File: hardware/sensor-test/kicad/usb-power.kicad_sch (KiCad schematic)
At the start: 12 parts, among them J1 TYPE-C-31-M-12, U10 USBLC6-2SC6, U3 AP2112K-3.3TRG1

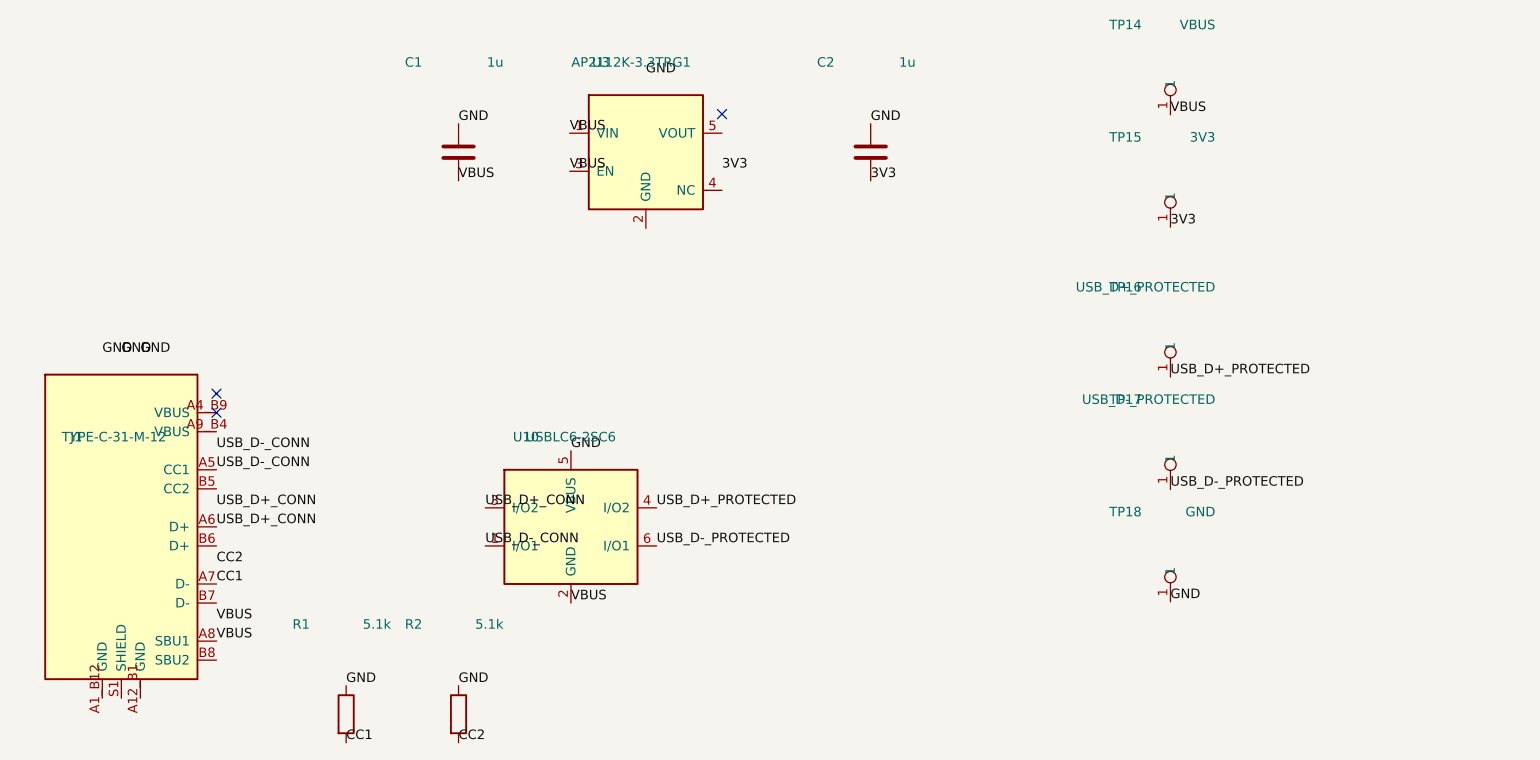
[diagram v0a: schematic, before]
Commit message: Fix USB-C pin coordinates and ERC power source
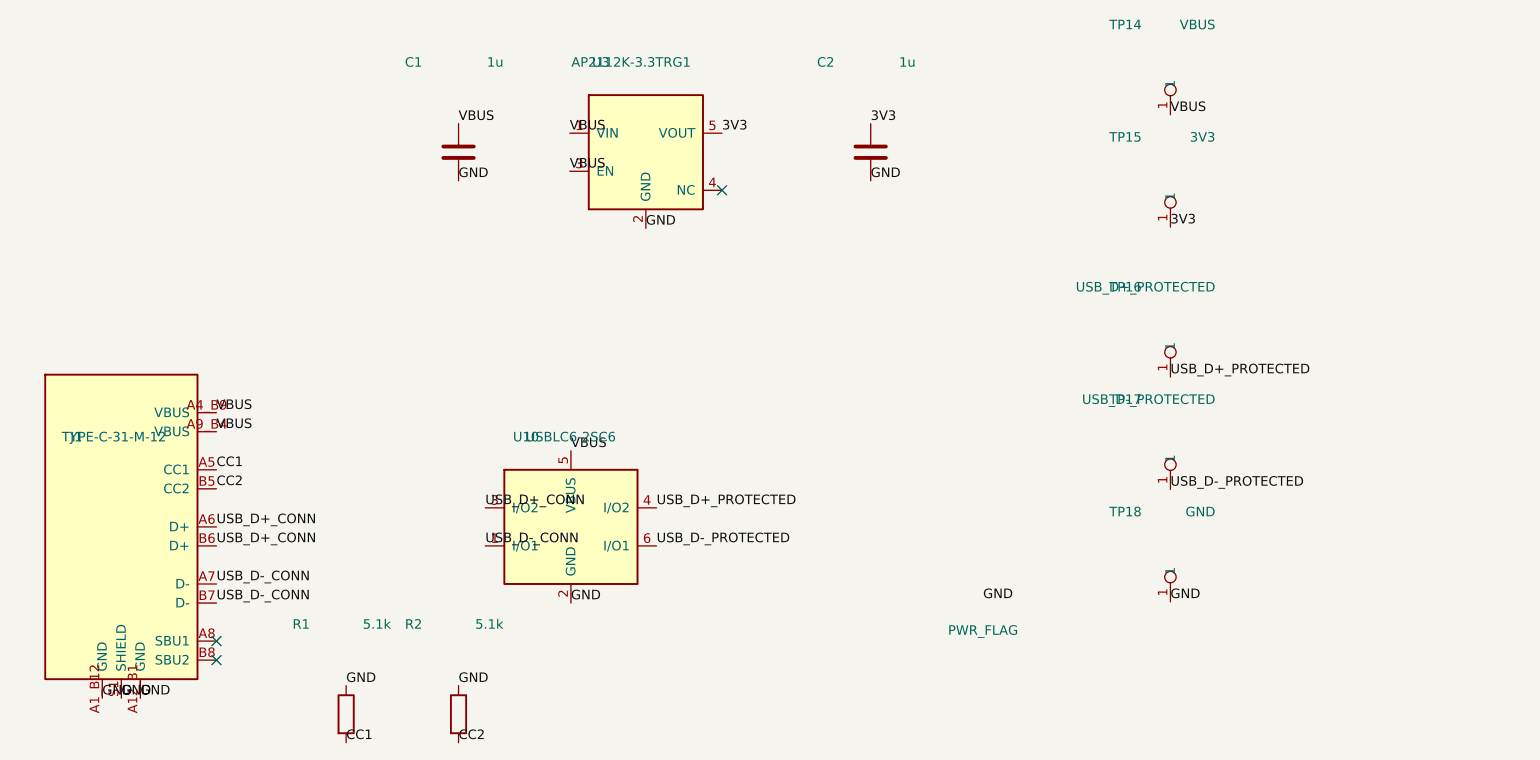
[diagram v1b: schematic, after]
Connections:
- net 3V3: now also C2.1, U3.5 (VOUT); no longer C2.2
- net CC1: now also J1.A5 (CC1); no longer J1.A7 (D-)
- net CC2: now also J1.B5 (CC2)
- net GND: now also C1.2, C2.2, J1.A12_B1 (GND), J1.A1_B12 (GND), J1.S1 (SHIELD), U10.2 (GND), U3.2 (GND); no longer C1.1, C2.1, U10.5 (VBUS)
- net USB_D+_CONN: now also J1.B6 (D+)
- net USB_D-_CONN: now also J1.A7 (D-), J1.B7 (D-); no longer J1.A5 (CC1)
- net VBUS: now also C1.1, J1.A4_B9 (VBUS), J1.A9_B4 (VBUS), U10.5 (VBUS); no longer C1.2, J1.A8 (SBU1), U10.2 (GND)
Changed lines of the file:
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@@
     (company "HE Piantor 42")
   )
-  (no_connect (at 57.7 84.76))
-  (no_connect (at 57.7 82.22))
-  (no_connect (at 125.16 44.92))
-  (label "VBUS" (at 57.7 115.24 0) (effects (font (size 1.27 1.27)) (justify left bottom)))
-  (label "VBUS" (at 57.7 112.7 0) (effects (font (size 1.27 1.27)) (justify left bottom)))
-  (label "CC1" (at 57.7 107.62 0) (effects (font (size 1.27 1.27)) (justify left bottom)))
-  (label "CC2" (at 57.7 105.08 0) (effects (font (size 1.27 1.27)) (justify left bottom)))
+  (no_connect (at 57.7 115.24))
+  (no_connect (at 57.7 117.78))
+  (no_connect (at 125.16 55.08))
+  (label "VBUS" (at 57.7 84.76 0) (effects (font (size 1.27 1.27)) (justify left bottom)))
+  (label "VBUS" (at 57.7 87.3 0) (effects (font (size 1.27 1.27)) (justify left bottom)))
+  (label "CC1" (at 57.7 92.38 0) (effects (font (size 1.27 1.27)) (justify left bottom)))
+  (label "CC2" (at 57.7 94.92 0) (effects (font (size 1.27 1.27)) (justify left bottom)))
   (label "USB_D+_CONN" (at 57.7 100 0) (effects (font (size 1.27 1.27)) (justify left bottom)))
-  (label "USB_D+_CONN" (at 57.7 97.46 0) (effects (font (size 1.27 1.27)) (justify left bottom)))
-  (label "USB_D-_CONN" (at 57.7 92.38 0) (effects (font (size 1.27 1.27)) (justify left bottom)))
-  (label "USB_D-_CONN" (at 57.7 89.84 0) (effects (font (size 1.27 1.27)) (justify left bottom)))
-  (label "GND" (at 42.46 77.14 0) (effects (font (size 1.27 1.27)) (justify left bottom)))
-  (label "GND" (at 47.54 77.14 0) (effects (font (size 1.27 1.27)) (justify left bottom)))
-  (label "GND" (at 45 77.14 0) (effects (font (size 1.27 1.27)) (justify left bottom)))
+  (label "USB_D+_CONN" (at 57.7 102.54 0) (effects (font (size 1.27 1.27)) (justify left bottom)))
+  (label "USB_D-_CONN" (at 57.7 107.62 0) (effects (font (size 1.27 1.27)) (justify left bottom)))
+  (label "USB_D-_CONN" (at 57.7 110.16 0) (effects (font (size 1.27 1.27)) (justify left bottom)))
+  (label "GND" (at 42.46 122.86 0) (effects (font (size 1.27 1.27)) (justify left bottom)))
+  (label "GND" (at 47.54 122.86 0) (effects (font (size 1.27 1.27)) (justify left bottom)))
+  (label "GND" (at 45 122.86 0) (effects (font (size 1.27 1.27)) (justify left bottom)))
   (label "CC1" (at 75 128.81 0) (effects (font (size 1.27 1.27)) (justify left bottom)))
   (label "GND" (at 75 121.19 0) (effects (font (size 1.27 1.27)) (justify left bottom)))
@@
   (label "USB_D-_CONN" (at 93.57 102.54 0) (effects (font (size 1.27 1.27)) (justify left bottom)))
   (label "USB_D-_PROTECTED" (at 116.43 102.54 0) (effects (font (size 1.27 1.27)) (justify left bottom)))
-  (label "VBUS" (at 105 110.16 0) (effects (font (size 1.27 1.27)) (justify left bottom)))
-  (label "GND" (at 105 89.84 0) (effects (font (size 1.27 1.27)) (justify left bottom)))
+  (label "VBUS" (at 105 89.84 0) (effects (font (size 1.27 1.27)) (justify left bottom)))
+  (label "GND" (at 105 110.16 0) (effects (font (size 1.27 1.27)) (justify left bottom)))
   (label "VBUS" (at 104.84 52.54 0) (effects (font (size 1.27 1.27)) (justify left bottom)))
   (label "VBUS" (at 104.84 47.46 0) (effects (font (size 1.27 1.27)) (justify left bottom)))
-  (label "GND" (at 115 39.84 0) (effects (font (size 1.27 1.27)) (justify left bottom)))
-  (label "3V3" (at 125.16 52.54 0) (effects (font (size 1.27 1.27)) (justify left bottom)))
-  (label "VBUS" (at 90 53.81 0) (effects (font (size 1.27 1.27)) (justify left bottom)))
-  (label "GND" (at 90 46.19 0) (effects (font (size 1.27 1.27)) (justify left bottom)))
-  (label "3V3" (at 145 53.81 0) (effects (font (size 1.27 1.27)) (justify left bottom)))
-  (label "GND" (at 145 46.19 0) (effects (font (size 1.27 1.27)) (justify left bottom)))
+  (label "GND" (at 115 60.16 0) (effects (font (size 1.27 1.27)) (justify left bottom)))
+  (label "3V3" (at 125.16 47.46 0) (effects (font (size 1.27 1.27)) (justify left bottom)))
+  (label "VBUS" (at 90 46.19 0) (effects (font (size 1.27 1.27)) (justify left bottom)))
+  (label "GND" (at 90 53.81 0) (effects (font (size 1.27 1.27)) (justify left bottom)))
+  (label "3V3" (at 145 46.19 0) (effects (font (size 1.27 1.27)) (justify left bottom)))
+  (label "GND" (at 145 53.81 0) (effects (font (size 1.27 1.27)) (justify left bottom)))
   (symbol (lib_id "HEP:HRO_TYPE-C-31-M-12") (at 45 100 0) (unit 1)
     (in_bom yes) (on_board yes) (dnp no)
@@
   )
   (label "GND" (at 185 110 0) (effects (font (size 1.27 1.27)) (justify left bottom)))
-  (sheet_instances
+(symbol (lib_id "power:PWR_FLAG") (at 160 110 0) (unit 1)
+    (in_bom yes) (on_board yes) (dnp no)
+    (property "Reference" "#FLG01" (at 160 111.905 0) (effects (font (size 1.27 1.27)) hide))
+    (property "Value" "PWR_FLAG" (at 160 113.81 0) (effects (font (size 1.27 1.27))))
+    (property "Footprint" "" (at 160 110 0) (effects (font (size 1.27 1.27)) hide))
+    (property "Datasheet" "~" (at 160 110 0) (effects (font (size 1.27 1.27)) hide))
+    (pin "1")
+    (instances
+      (project "usb-power"
+        (path "/c0000000-0000-0000-0000-000000000001"
+          (reference "#FLG01") (unit 1)
+        )
+      )
+    )
+  )
+  (label "GND" (at 160 110 0)
+    (effects (font (size 1.27 1.27)) (justify left bottom))
+  )
+    (sheet_instances
     (path "/" (page "1"))
   )

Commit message: Model USB VBUS source correctly for ERC
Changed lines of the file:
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@@
+    (effects (font (size 1.27 1.27)) (justify left bottom))
+  )
+  (symbol (lib_id "power:PWR_FLAG") (at 170 45 0) (unit 1)
+    (in_bom yes) (on_board yes) (dnp no)
+    (property "Reference" "#FLG02" (at 170 46.905 0) (effects (font (size 1.27 1.27)) hide))
+    (property "Value" "PWR_FLAG" (at 170 48.81 0) (effects (font (size 1.27 1.27))))
+    (property "Footprint" "" (at 170 45 0) (effects (font (size 1.27 1.27)) hide))
+    (property "Datasheet" "~" (at 170 45 0) (effects (font (size 1.27 1.27)) hide))
+    (pin "1")
+    (instances
+      (project "usb-power"
+        (path "/c0000000-0000-0000-0000-000000000001"
+          (reference "#FLG02") (unit 1)
+        )
+      )
+    )
+  )
+  (label "VBUS" (at 170 45 0)
     (effects (font (size 1.27 1.27)) (justify left bottom))
   )

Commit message: Add independent 3V3 power LED
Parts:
- added D1: POWER_GREEN, LED_SMD:LED_0603_1608Metric, symbol HEP:LED
- added R10: 1.5k, Resistor_SMD:R_0603_1608Metric, symbol Device:R
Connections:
- net 3V3: now also R10.1
- net GND: now also D1.2 (A)
- new net PWR_LED_A: D1.1 (K), R10.2
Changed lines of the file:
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@@
     (effects (font (size 1.27 1.27)) (justify left bottom))
   )
-    (sheet_instances
+  (symbol (lib_id "Device:R") (at 220 50 0) (unit 1)
+    (in_bom yes) (on_board yes) (dnp no)
+    (property "Reference" "R10" (at 223 50 90) (effects (font (size 1.27 1.27))))
+    (property "Value" "1.5k" (at 217 50 90) (effects (font (size 1.27 1.27))))
+    (property "Footprint" "Resistor_SMD:R_0603_1608Metric" (at 220 50 0) (effects (font (size 1.27 1.27)) hide))
+    (property "Datasheet" "~" (at 220 50 0) (effects (font (size 1.27 1.27)) hide))
+    (pin "1")
+    (pin "2")
+    (instances (project "usb-power" (path "/c0000000-0000-0000-0000-000000000001" (reference "R10") (unit 1))))
+  )
+  (label "3V3" (at 220 46.19 0) (effects (font (size 1.27 1.27)) (justify left bottom)))
+  (label "PWR_LED_A" (at 220 53.81 0) (effects (font (size 1.27 1.27)) (justify left bottom)))
+  (symbol (lib_id "HEP:LED") (at 220 65 0) (unit 1)
+    (in_bom yes) (on_board yes) (dnp no)
+    (property "Reference" "D1" (at 223 65 90) (effects (font (size 1.27 1.27))))
+    (property "Value" "POWER_GREEN" (at 217 65 90) (effects (font (size 1.27 1.27))))
+    (property "Footprint" "LED_SMD:LED_0603_1608Metric" (at 220 65 0) (effects (font (size 1.27 1.27)) hide))
+    (property "Datasheet" "~" (at 220 65 0) (effects (font (size 1.27 1.27)) hide))
+    (pin "1")
+    (pin "2")
+    (instances (project "usb-power" (path "/c0000000-0000-0000-0000-000000000001" (reference "D1") (unit 1))))
+  )
+  (label "PWR_LED_A" (at 220 61.19 0) (effects (font (size 1.27 1.27)) (justify left bottom)))
+  (label "GND" (at 220 68.81 0) (effects (font (size 1.27 1.27)) (justify left bottom)))
+  (sheet_instances
     (path "/" (page "1"))
   )
